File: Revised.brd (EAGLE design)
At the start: 22.3 x 64 mm, 17 parts, among them IC1 ATMEGA328P_PDIP

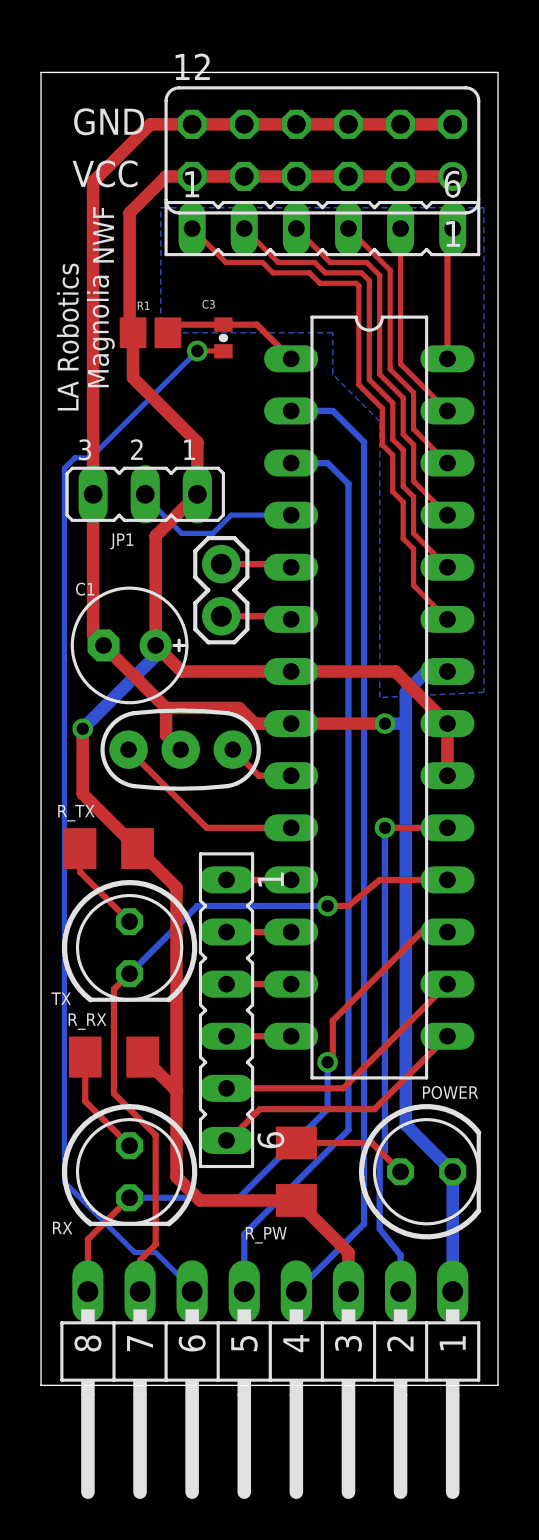
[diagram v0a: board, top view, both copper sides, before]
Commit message: Small tweaks
Remove capacitive coupling to RST#, which should enable debugWIRE
Thicken the power and ground traces, tweaking routes for clearance
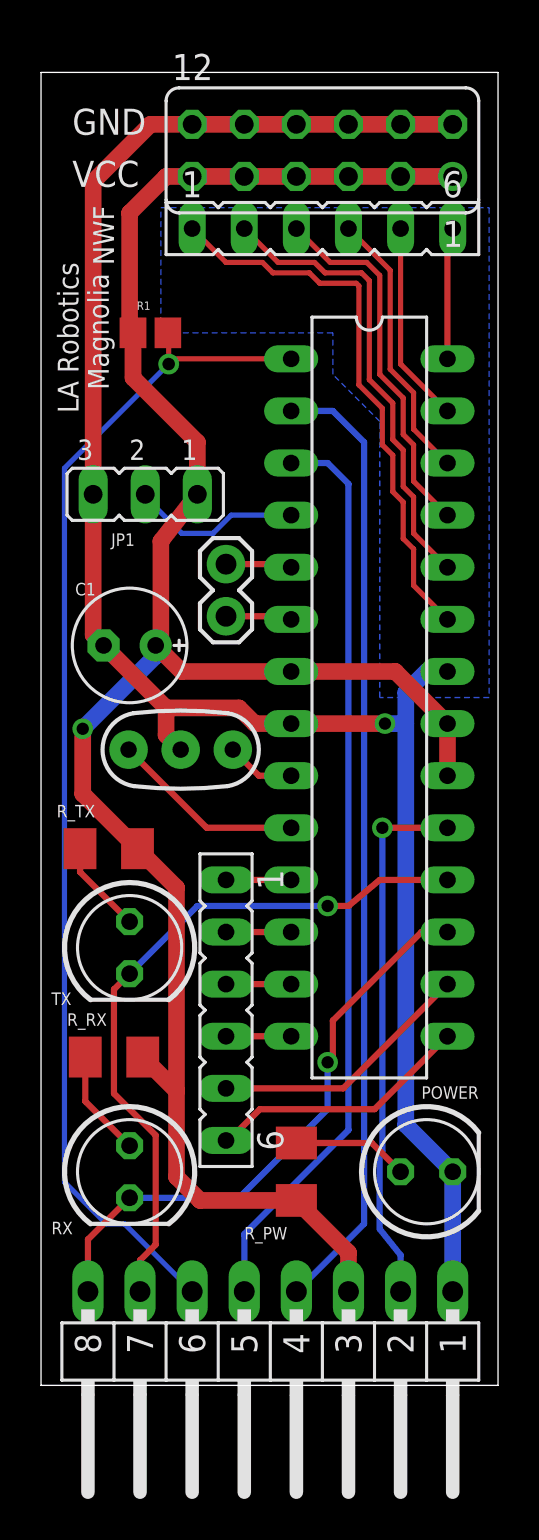
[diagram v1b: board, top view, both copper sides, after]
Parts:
- removed C3: 0.1uF, SparkFun:0402-CAP
- moved IO2 0.23 mm to (9.02, 40.0)
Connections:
- removed net N$3: C3.2, IC1.1, R1.1
- net RTS#: now also IC1.1, R1.1; no longer C3.1
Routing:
- net N$3: track 6.86 -> 0.00 mm
- net RTS#: track 53.4 -> 58.5 mm

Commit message: Cleanup
Change IO2 header pinouts to include the entire SPI bus
Move LEDs to PD5 (T1) and PB0 (ICP)
Move PB1 (OC1A) to CTS# connector
Redo some traces to avoid vias
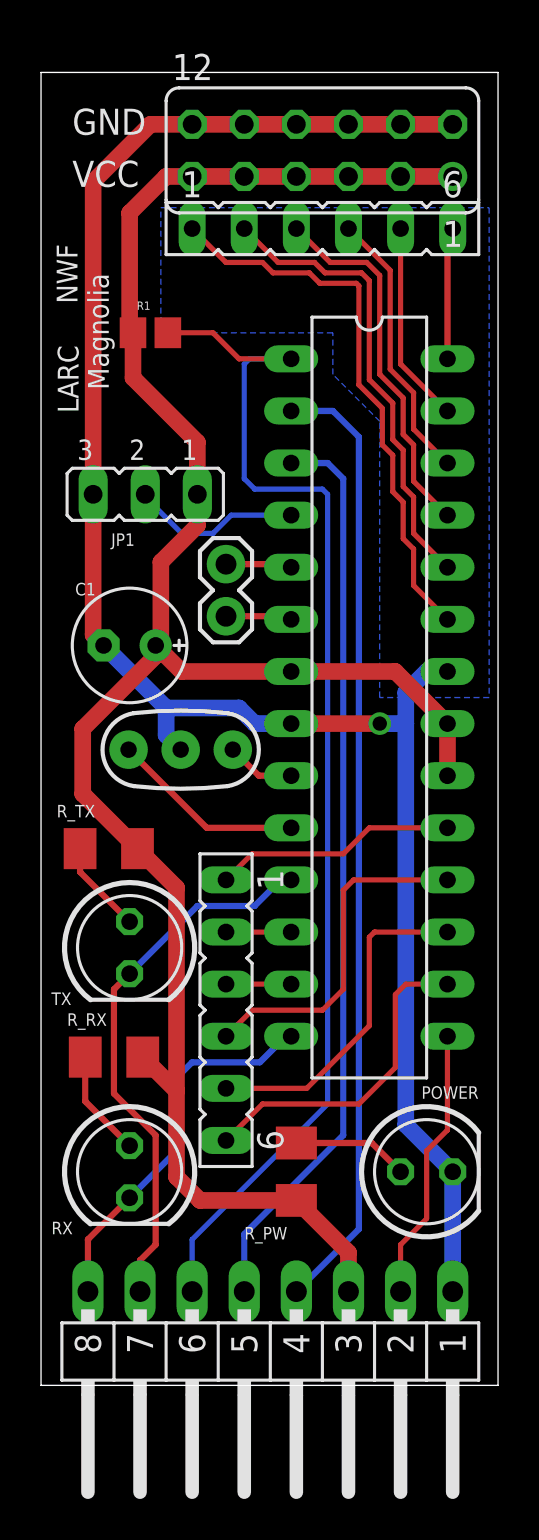
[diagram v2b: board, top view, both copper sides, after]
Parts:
- renumbered ADC1 to ADC, ADCSUPPLY to PWR, SV1 to SER
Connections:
- net N$10 renamed PD6|AIN0
- net N$11 renamed PD7|AIN1
- net N$7 renamed PD3|INT1
- net N$8 renamed PD4|T0
- net POWER renamed VCC
- removed net N$12: IC1.14, IO1.4
- removed net N$13: IC1.15, IO1.6
- removed net N$14: IC1.16, IO1.5
- removed net N$9: IC1.11, IO1.1
- new net PB2|SS: IC1.16, IO1.6
- new net PB3|MOSI: IC1.17, IO1.5
- new net PB4|MISO: IC1.18, IO1.4
- new net PB5|SCK: IC1.19, IO1.1
- net CTS#: now also IC1.15; no longer IC1.19
- net RXLED: now also IC1.14; no longer IC1.17
- net TXLED: now also IC1.11; no longer IC1.18
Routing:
- net PB4|MISO: track 0.00 -> 16.8 mm
- net PB3|MOSI: track 0.00 -> 16.5 mm
- net PB2|SS: track 0.00 -> 16.0 mm
- net N$13: track 12.9 -> 0.00 mm
- net N$14: track 12.9 -> 0.00 mm
- net CTS#: track 26.2 -> 13.4 mm, vias 1 -> 0
- net PB5|SCK: track 0.00 -> 11.8 mm
- net RXLED: track 28.7 -> 18.6 mm, vias 1 -> 0
- net TXLED: track 34.3 -> 26.7 mm, vias 1 -> 0
- net N$9: track 3.18 -> 0.00 mm
- net N$12: track 3.18 -> 0.00 mm
- net RTS#: track 58.5 -> 60.5 mm, vias 1 -> 0
- net VCC: track 101.6 -> 101.7 mm, vias 1 -> 0
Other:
- board text added: "LARC"
- board text removed: "LA Robotics"

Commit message: Ground plane, better analog pin routing?
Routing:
- net GND: track 92.7 -> 5.84 mm, vias 1 -> 0
- net TXD: track 46.7 -> 48.2 mm
- net RXD: track 44.5 -> 45.7 mm
- net A3: track 13.4 -> 14.5 mm
- net A1: track 22.7 -> 23.7 mm
- net A4: track 9.84 -> 10.7 mm
- net A2: track 18.1 -> 18.8 mm
- net RTS#: track 60.5 -> 61.1 mm
